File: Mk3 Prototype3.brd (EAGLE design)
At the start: 121.6 x 70 mm, 152 parts, among them IC1 TPD3E001DRL, IC2 TPS62082, IC3 STM32F401V, IC4 BQ24092, IC6 CC3100MOD, IC7 BQ2970, IC8 LSM6DS3, IC9 LIS3MDL, J1 ZX62-AB-5PA(11), J2 ER-CON50HT-1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

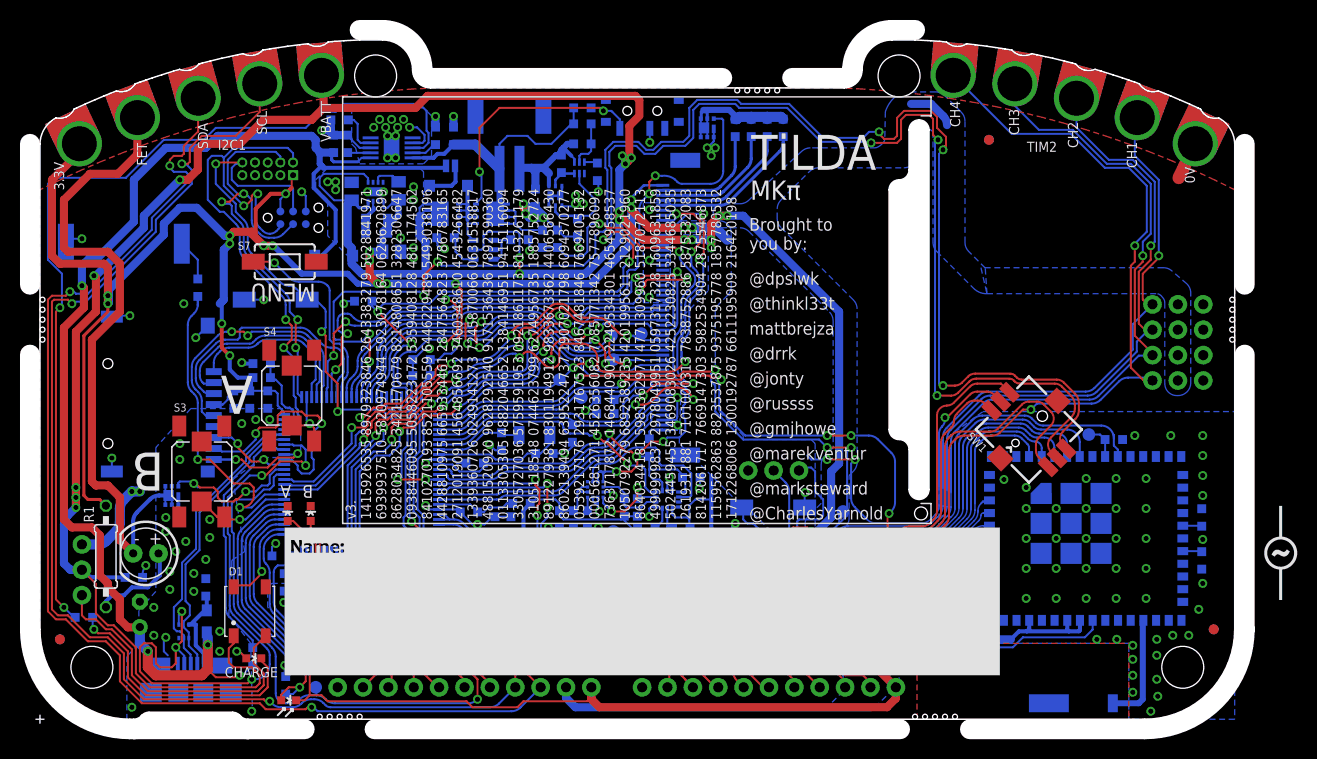
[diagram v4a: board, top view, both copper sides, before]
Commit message: Revert Prototype3 files to as sent for PCB fab
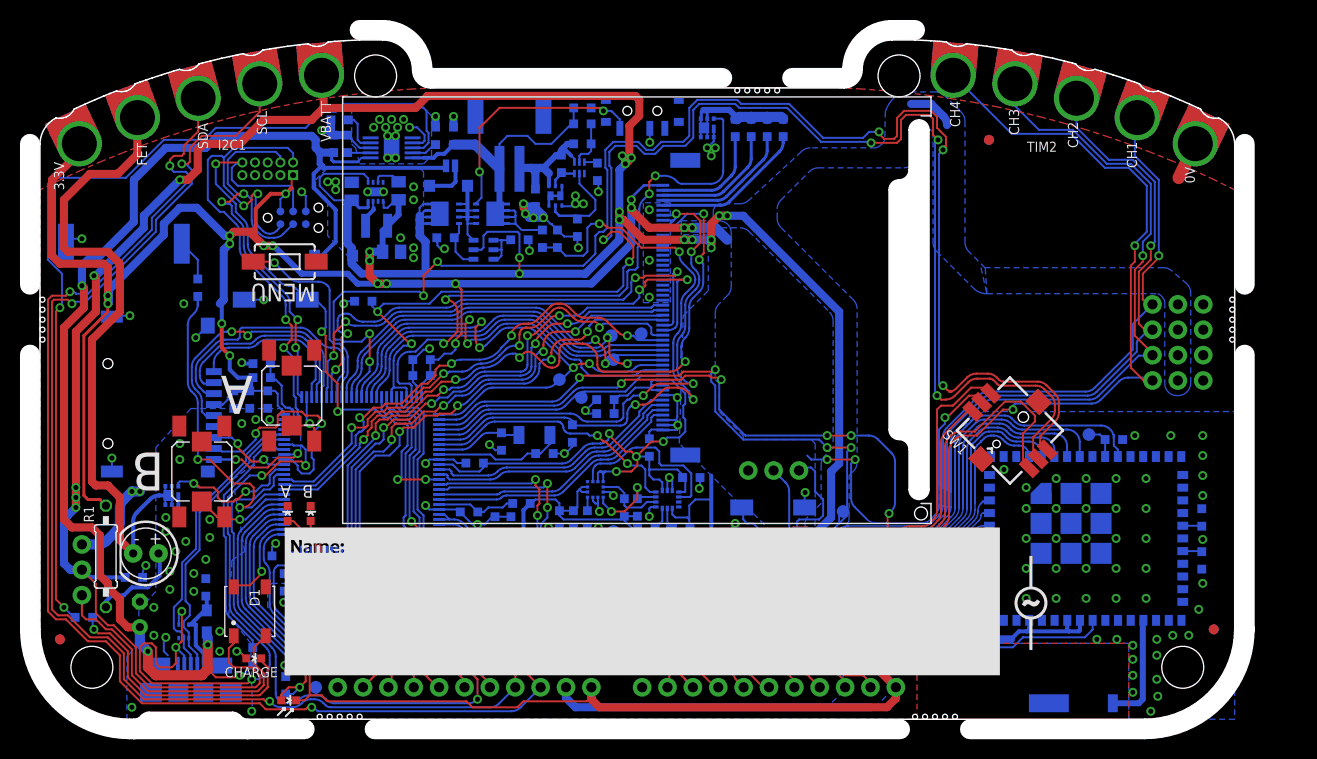
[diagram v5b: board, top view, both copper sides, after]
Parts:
- JP3: value JST PH 2mm -> (none)
- R11: value DNP -> DNP / 0603/100K/5%
- R32: value DNP (0603/0R/5%) -> DNP (0)
- R44, R47, R48, R49: value 0603/12R/5% -> 0603/4R7/5%
- moved U$5 25.5 mm to (99.2, 11.6)
- moved SW1 1.90 mm to (97.1, 28.9)
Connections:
- net VABT_SWTICHED renamed N$16
- net VBAT_NEG renamed N$57
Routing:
- net JOY_DOWN: track 110.1 -> 107.2 mm
- net +3V3: track 547.7 -> 545.7 mm
- net BOOT0: track 149.0 -> 147.3 mm
- net JOY_LEFT: track 111.0 -> 109.3 mm
- net JOY_UP: track 121.0 -> 120.0 mm
- net N$16: track 12.5 -> 13.3 mm
- net JOY_RIGHT: track 147.3 -> 146.6 mm
- net CC_HIB: track 129.4 -> 128.8 mm
- net GND: vias 154 -> 155
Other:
- board text added: "PB11"
- board text removed: "@CharlesYarnold"
- board text removed: "@dpslwk"
- board text removed: "@drrk"
- board text removed: "@gmjhowe"
- board text removed: "@jonty"
- board text removed: "@marekventur"
- board text removed: "@marksteward"
- board text removed: "@russss"
- board text removed: "@thinkl33t"
- board text removed: "Brought to you by:"
- board text removed: "MKπ"
- board text removed: "PB2"
- board text removed: "TiLDA"
- board text removed: "mattbrejza"
- board text removed: "v3. 1415926535 8979323846 2643383279 5028841971 6939937510 5820974944 5923078164 0628620899 8628034825 3421170679 8214808651 3282306647 0938446095 5058223172 5359408128 4811174502 8410270193 8521105559 6446229489 5493038196 4428810975 6659334461 2847564823 3786783165 2712019091 4564856692 3460348610 4543266482 1339360726 0249141273 7245870066 0631558817 4881520920 9628292540 9171536436 7892590360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"
